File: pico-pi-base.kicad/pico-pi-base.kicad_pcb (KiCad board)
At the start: 2 copper layers, 65 x 56 mm, 15 parts, among them J1 GPIO, J2 JST-PH2 Bat Ext, J3 Grove, J4 JST-PH2 Bat Int, J5 Conn_SPI1, SW1 SW_Push, U1 Pico_nodbg

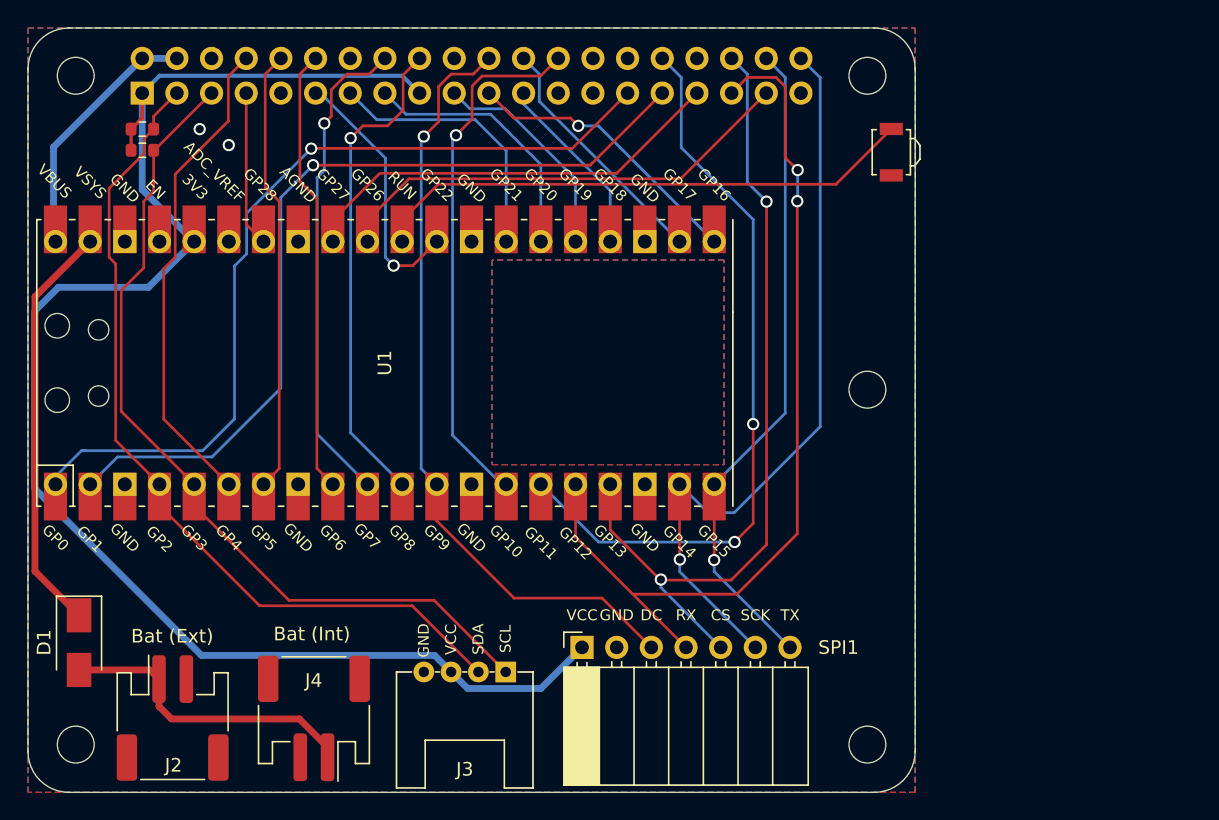
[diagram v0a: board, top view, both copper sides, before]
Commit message: pico-pi-base Rev 1.2
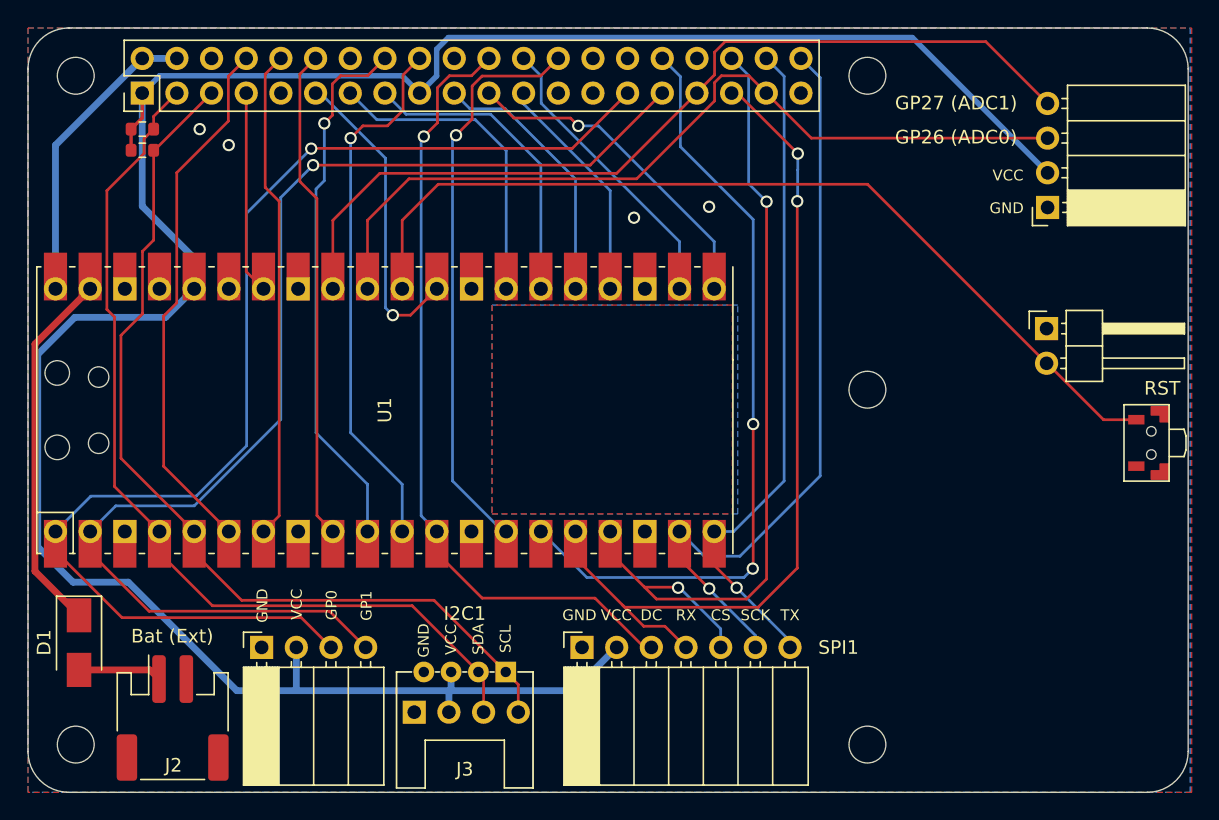
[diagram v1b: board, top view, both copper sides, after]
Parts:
- added J6: Conn_ADC, Connector_PinSocket_2.54mm:PinSocket_1x04_P2.54mm_Horizontal, F.Cu at (174.7, 57.1)
- added J7: Conn_RST, Connector_PinHeader_2.54mm:PinHeader_1x02_P2.54mm_Horizontal, F.Cu at (174.6, 66.0)
- added J8: Conn_I2C, Connector_PinHeader_2.54mm:PinHeader_1x04_P2.54mm_Horizontal, B.Cu at (128.3, 94.1)
- J1: footprint Connector_PinSocket_2.54mm:PinSocket_2x20_P2.54mm_Vertical -> Connector_PinHeader_2.54mm:PinHeader_2x20_P2.54mm_Vertical; moved to F.Cu
- J4: value JST-PH2 Bat Int -> Conn_UART; footprint Connector_JST:JST_PH_S2B-PH-SM4-TB_1x02-1MP_P2.00mm_Horizontal -> Connector_PinSocket_2.54mm:PinSocket_1x04_P2.54mm_Horizontal
- SW1: footprint Button_Switch_SMD:SW_SPST_B3U-3000P -> user:Microtaster_Horizontal
- moved SW1 28.6 mm to (182.3, 74.4), turned to 90 degrees
- moved J4 6.46 mm to (117.1, 89.4), turned to 90 degrees
- moved U1 3.46 mm to (126.1, 72.0)
- turned J1 to 90 degrees
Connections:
- J4 pad 1: +BATT -> GND
- J4 pad 2: GND -> +3.3V
- J5 pad 1: +3.3V -> GND
- J5 pad 2: GND -> +3.3V
- SW1 pad 1: /RUN -> GND
- SW1 pad 2: GND -> /RUN
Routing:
- net +3.3V: track 112.6 -> 176.2 mm
- net /GPIO[13]/PWM1: track 32.1 -> 65.7 mm
- net /GPIO26: track 34.6 -> 61.9 mm
- net /RUN: track 40.2 -> 67.0 mm
- net /GPIO[6]: track 62.0 -> 87.8 mm
- net /GPIO[5]: track 62.6 -> 88.3 mm
- net +BATT: track 22.5 -> 6.14 mm
- net /GPIO[3]/SCL1: track 63.1 -> 68.5 mm
- net /GPIO[2]/SDA1: track 62.2 -> 67.5 mm
- net /GPIO[17]: track 19.1 -> 22.8 mm
- net /GPIO[23]: track 35.7 -> 39.5 mm
- net /GPIO[14]/TXD0: track 35.7 -> 39.1 mm
- net /GPIO[19]/PCM.FS: track 66.9 -> 63.5 mm
- net /GPIO[8]/SPI0.CE0: track 18.2 -> 21.6 mm
- net /GPIO[11]/SPI0.SCLK: track 13.5 -> 17.0 mm
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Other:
- board size 65 x 56 mm -> 85 x 56 mm
- board text added: "GP0"
- board text added: "GP1"
- board text added: "GP26 (ADC0)"
- board text added: "GP27 (ADC1)"
- board text added: "I2C1"
- board text added: "RST"
- board text added: "SCL"
- board text added: "SDA"
- board text added: "https://github.com/bablokb/pcb-pico-pi-base Rev 1.2"
- board text removed: "Bat (Int)"

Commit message: Rev 2.0: swapped pins to support I2S
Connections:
- U1 pad 10: /GPIO[23] -> /GPIO[18]/PCM.CLK
- U1 pad 11: /GPIO[24] -> /GPIO[19]/PCM.FS
- U1 pad 15: /GPIO[12]/PWM0 -> /GPIO[24]
- U1 pad 16: /GPIO[19]/PCM.FS -> /GPIO[12]/PWM0
- U1 pad 9: /GPIO[18]/PCM.CLK -> /GPIO[23]
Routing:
- net /GPIO[24]: track 39.4 -> 54.7 mm
- net /GPIO[19]/PCM.FS: track 63.5 -> 74.2 mm
- net /GPIO[25]: track 58.3 -> 60.4 mm
- net /GPIO[18]/PCM.CLK: track 36.1 -> 37.2 mm
- net /GPIO[23]: track 39.5 -> 38.4 mm
- net /GPIO[12]/PWM0: track 57.3 -> 56.5 mm
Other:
- board text added: "https://github.com/bablokb/pcb-pico-pi-base Rev 2.0"
- board text removed: "https://github.com/bablokb/pcb-pico-pi-base Rev 1.2"

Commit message: Rev 2.1: add MicroSD-BFF
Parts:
- added JP1: ADC0/SD_CS, Jumper:SolderJumper-3_P1.3mm_Bridged12_Pad1.0x1.5mm, F.Cu at (168.6, 56.0)
- added U2: SD-BFF, user:SD_BFF, F.Cu at (182.6, 96.3)
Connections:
- J6 pad 3: /GPIO26 -> /ADC0
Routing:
- net /GPIO[11]/SPI0.SCLK: track 17.0 -> 82.6 mm
- net /GPIO[10]/SPI0.MOSI: track 19.5 -> 82.9 mm, vias 0 -> 2
- net /GPIO[9]/SPI0.MISO: track 24.5 -> 76.5 mm
- net +3.3V: track 176.2 -> 208.9 mm
- net /SD_CS: track 0.00 -> 29.8 mm, vias 0 -> 1
- net /ADC0: track 0.00 -> 7.24 mm
- net /GPIO[19]/PCM.FS: track 74.2 -> 79.1 mm
- net /GPIO26: track 61.9 -> 57.4 mm
- net /GPIO[16]: track 60.9 -> 57.8 mm, vias 2 -> 1
- net /GPIO[21]/PCM.DOUT: track 55.5 -> 56.8 mm
- net /GPIO[20]/PCM.DIN: track 49.0 -> 49.9 mm
- net GND: vias 4 -> 11
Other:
- board text added: "ADC0"
- board text added: "SD"
- board text added: "https://github.com/bablokb/pcb-pico-pi-base Rev 2.1"
- board text removed: "RJ45"
- board text removed: "https://github.com/bablokb/pcb-pico-pi-base Rev 2.0"

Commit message: pico-pi-base: Rev. 2.2
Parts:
- removed U2: SD-BFF, user:SD_BFF
- added J9: Micro_SD_TF_PUSH, user:TF-Push, F.Cu at (175.0, 90.1)
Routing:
- net /GPIO[11]/SPI0.SCLK: track 82.6 -> 75.2 mm
- net /GPIO[9]/SPI0.MISO: track 76.5 -> 69.6 mm
- net /GPIO[10]/SPI0.MOSI: track 82.9 -> 76.4 mm, vias 2 -> 0
- net /SD_CS: track 29.8 -> 34.5 mm, vias 1 -> 2
- net +3.3V: track 208.9 -> 205.0 mm, vias 0 -> 1
- net GND: vias 11 -> 27
